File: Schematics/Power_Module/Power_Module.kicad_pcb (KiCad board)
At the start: 4 copper layers, 69.5 x 60 mm, 135 parts, among them J1 ScrewSwitch, J2 Battery, J3 ScrewSwitch, J4 GSE, J5 USB_C_Female_USB2_Small, J6 SWD_B, J7 Stack Male Edge Connector, Q1 AO4447A, Q2 TSM2309CX, Q3 DMN6040SSD-13, SW1 SW_STM_RESET, SW2 SW_STM_BOOT_MODE, U1 TPS61175PWPR, U10 LM66100DCKR, U11 LM66100DCKR, U12 AMS1117-3.3, U13 CP2102N-A02-GQFN20R, U14 STM32F103CBT6, U15 ISO1044BDR, U16 W25Q128JVS, U2 LM74700QDBVRQ1, U3 LM74700QDBVRQ1, U4 ACS37041KLHBLT-010B3, U5 ACS37041KLHBLT-010B5, U6 INA181A2, U7 LMR51430XDDCR, U8 LMR51430XDDCR, U9 LM66100DCKR, Y1 X322516MMB4SI

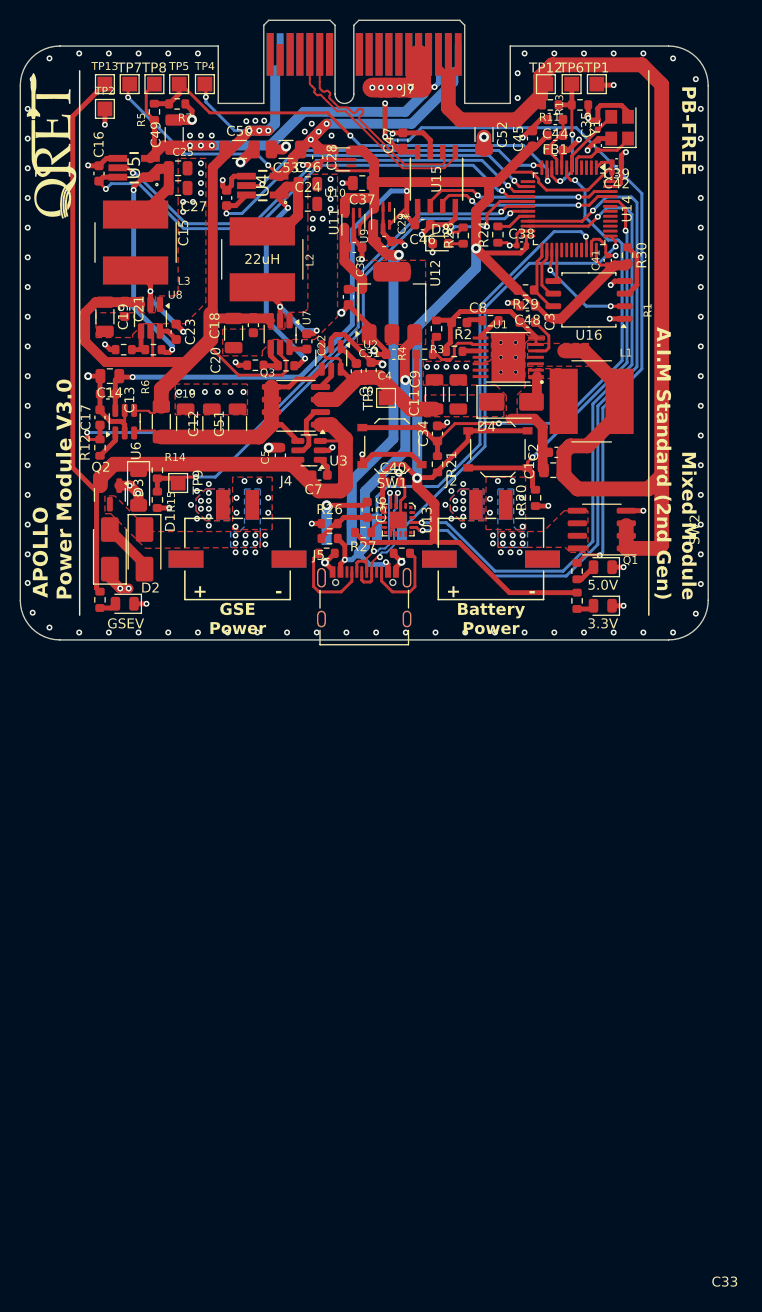
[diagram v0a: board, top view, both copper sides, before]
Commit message: hybrid power board, with preserved OG Power board  - still hybrid still needs review and silkscreen
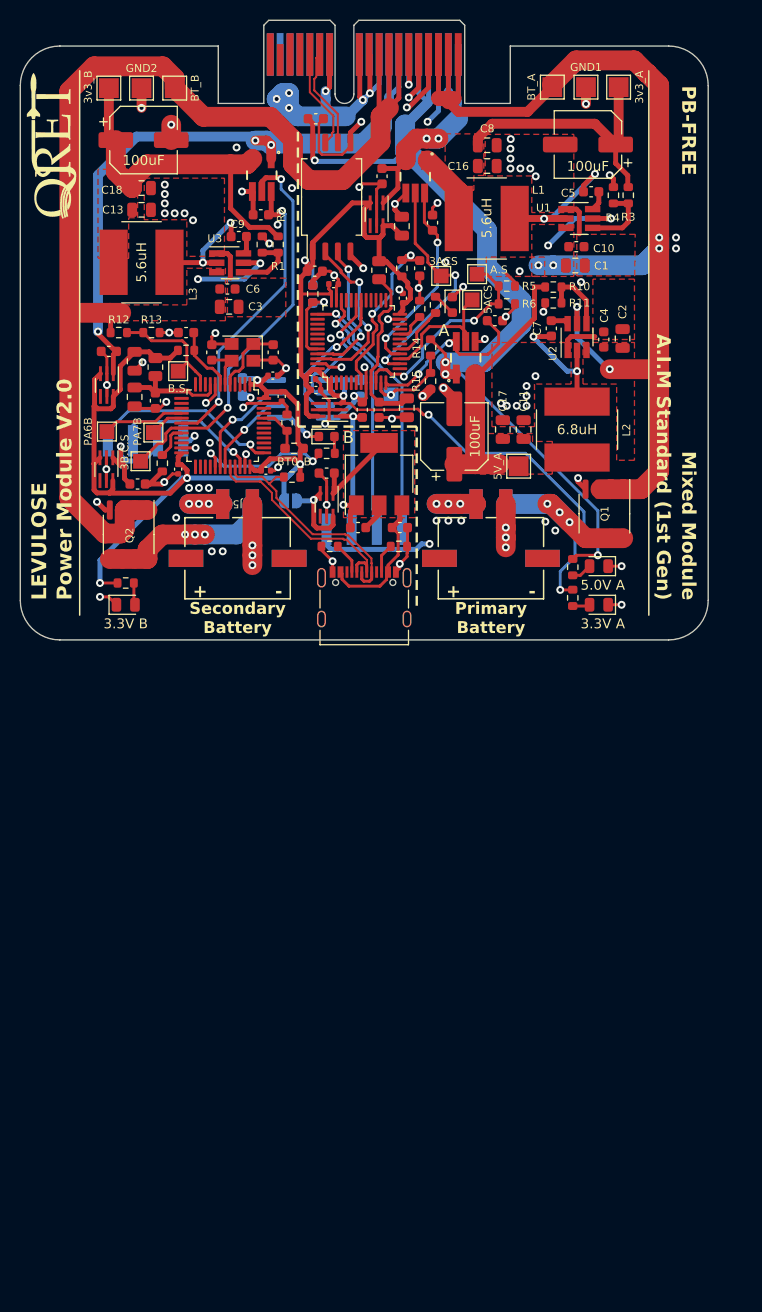
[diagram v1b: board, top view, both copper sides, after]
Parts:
- removed C51, C52, C53: 22uF, Capacitor_SMD:C_1206_3216Metric
- removed D4: 50V 3A, Diode_SMD:D_SMA
- removed D6: 5V PWR (RED), LED_SMD:LED_0805_2012Metric
- removed D7: 24V PWR (YLW), LED_SMD:LED_0805_2012Metric
- removed Q3: DMN6040SSD-13, Package_SO:SOIC-8_3.9x4.9mm_P1.27mm
- removed R29, R30: 10k, Resistor_SMD:R_0603_1608Metric
- removed SW1: SW_STM_RESET, Button_Switch_SMD:SW_Push_1P1T_XKB_TS-1187A
- removed SW2: SW_STM_BOOT_MODE, Button_Switch_SMD:SW_Push_1P1T_XKB_TS-1187A
- added FB2: 100R, Resistor_SMD:R_0805_2012Metric, F.Cu at (143.9, 72.2)
- added J8: SWD_B, SWD_Header:SWD_PinHeader_1x04_P2.54mm_Horizontal_SMD, B.Cu at (161.2, 88.6)
- added JP1: USB_V_EN, Jumper:SolderJumper-2_P1.3mm_Open_RoundedPad1.0x1.5mm, B.Cu at (157.6, 85.7)
- added TP10: B.S, TestPoint:TestPoint_Pad_1.5x1.5mm, F.Cu at (146.2, 72.6)
- added TP11: 3B.C.S, TestPoint:TestPoint_Pad_1.5x1.5mm, F.Cu at (142.4, 81.7)
- added TP16: PA7B, TestPoint:TestPoint_Pad_1.5x1.5mm, F.Cu at (143.7, 78.8)
- added TP17: PA6B, TestPoint:TestPoint_Pad_1.5x1.5mm, F.Cu at (139.0, 78.7)
- C10, C9: value 10uF -> 100nF; footprint Capacitor_SMD:C_1206_3216Metric -> Capacitor_SMD:C_0603_1608Metric
- C11, C18: value 10uF -> 22uF; footprint Capacitor_SMD:C_1206_3216Metric -> Capacitor_SMD:C_0805_2012Metric
- C12: value 22uF -> 100uF; footprint Capacitor_SMD:C_1206_3216Metric -> Capacitor_SMD:CP_Elec_6.3x5.9
- C13, C16, C17: value 100nF -> 22uF; footprint Capacitor_SMD:C_0603_1608Metric -> Capacitor_SMD:C_0805_2012Metric
- C14: value 4.7uF -> 100uF; footprint Capacitor_SMD:C_0805_2012Metric -> Capacitor_SMD:CP_Elec_6.3x5.9
- C15: value 100nF -> 100uF; footprint Capacitor_SMD:C_0603_1608Metric -> Capacitor_SMD:CP_Elec_6.3x5.9
- C19: footprint Capacitor_SMD:C_1206_3216Metric -> Capacitor_SMD:C_0603_1608Metric
- C2: value 100nF -> 4.7uF; footprint Capacitor_SMD:C_0603_1608Metric -> Capacitor_SMD:C_0805_2012Metric
- C20: value 100nF -> 10uF
- C21, C22, C46: value 100nF -> 0.1u
- C23: value 100nF -> 10p
- C24: value 10uF -> 10p; footprint Capacitor_SMD:C_0805_2012Metric -> Capacitor_SMD:C_0603_1608Metric
- C25, C26, C27: value 10uF -> 100n; footprint Capacitor_SMD:C_0805_2012Metric -> Capacitor_SMD:C_0402_1005Metric
- C28, C29, C30: value 1uF -> 100n; footprint Capacitor_SMD:C_0603_1608Metric -> Capacitor_SMD:C_0402_1005Metric
- C3: value 10nF -> 4.7uF; footprint Capacitor_SMD:C_0603_1608Metric -> Capacitor_SMD:C_0805_2012Metric
- C31, C32: value 10uF -> 100n; footprint Capacitor_SMD:C_0603_1608Metric -> Capacitor_SMD:C_0402_1005Metric
- C33: value 10p -> 10n; footprint Capacitor_SMD:C_0402_1005Metric -> Capacitor_SMD:C_0603_1608Metric
- C34: value 100nF -> 1uF; footprint Capacitor_SMD:C_0603_1608Metric -> Capacitor_SMD:C_0805_2012Metric
- C35: value 10p -> 1uF; footprint Capacitor_SMD:C_0402_1005Metric -> Capacitor_SMD:C_0805_2012Metric
- C36: value 1uF -> 10n
- C37, C40: value 10uF -> 1uF
- C38: value 100n -> 1uF; footprint Capacitor_SMD:C_0402_1005Metric -> Capacitor_SMD:C_0805_2012Metric
- C39, C41, C42: value 100n -> 1uF; footprint Capacitor_SMD:C_0402_1005Metric -> Capacitor_SMD:C_0603_1608Metric
- C4, C5, C6, C7: value 1uF -> 100nF
- C43: value 10nF -> 1uF
- C44, C45: value 1uF -> 0.1u
- C49, C50: value 22uF -> 0.1u; footprint Capacitor_SMD:C_1206_3216Metric -> Capacitor_SMD:C_0603_1608Metric_Pad1.08x0.95mm_HandSolder; moved to B.Cu
- C8: value 33nF -> 22uF; footprint Capacitor_SMD:C_0603_1608Metric -> Capacitor_SMD:C_0805_2012Metric
- D1: value SMAJ30A -> 3.3V_A PWR (GRN); footprint Diode_SMD:D_SMA -> LED_SMD:LED_0805_2012Metric
- D2: value SMAJ30A -> 5.0V_A PWR (RED); footprint Diode_SMD:D_SMA -> LED_SMD:LED_0805_2012Metric
- D3: value BZV55C12 -> 3.3V_B PWR (GRN); footprint Diode_SMD:D_MiniMELF -> LED_SMD:LED_0805_2012Metric
- D5: value 3.3V PWR (GRN) -> DB_LED (YLW); footprint LED_SMD:LED_0805_2012Metric -> LED_SMD:LED_0603_1608Metric
- FB1: footprint Inductor_SMD:L_0603_1608Metric -> Resistor_SMD:R_0805_2012Metric
- J1: value ScrewSwitch -> ScrewSwitch B
- J2: value Battery -> ScrewSwitch A; moved to B.Cu
- J3: value ScrewSwitch -> Battery A; moved to F.Cu
- J4: value GSE -> USB_C_Female_USB2_Small; footprint footprints:CONN_2-1445057-2_TYCO -> footprints:USB_C_DB-108PWB
- J5: value USB_C_Female_USB2_Small -> Battery B; footprint footprints:USB_C_DB-108PWB -> footprints:CONN_2-1445057-2_TYCO
- J6: value SWD_B -> Stack Male Edge Connector; footprint SWD_Header:SWD_PinHeader_1x04_P2.54mm_Horizontal_SMD -> Connector_PCBEdge:BUS_PCIexpress_x1; moved to F.Cu
- J7: value Stack Male Edge Connector -> SWD_B; footprint Connector_PCBEdge:BUS_PCIexpress_x1 -> SWD_Header:SWD_PinHeader_1x04_P2.54mm_Horizontal_SMD; moved to B.Cu
- L1: value 47uH -> 5.6uH
- L2: value 22uH -> 6.8uH
- L3: value 68uH -> 5.6uH
- Q2: value TSM2309CX -> AO4447A; footprint Package_TO_SOT_SMD:SOT-23 -> Package_SO:SOIC-8_3.9x4.9mm_P1.27mm
- R1: value 6.2k -> 100k
- R10: value 12K -> 56k
- R11: value 30k -> 7.5k
- R12: value 1k -> 30k
- R14: value 10k -> 30k
- R15: value 100k -> 30k
- R16: value 100k -> 1.5k
- R17: value 22k -> 5.1k
- R18: value 56k -> 5.1k
- R19: value 7.5k -> 680R
- R2: value 82k -> 22k
- R20: value 100k -> 680R
- R21: value 100k -> 10k
- R22: value 5.1k -> 10k
- R23: value 5.1k -> 100k
- R24: value 100k -> BT0_A; footprint Resistor_SMD:R_0603_1608Metric -> Resistor_SMD:R_0603_1608Metric_Pad0.98x0.95mm_HandSolder; moved to B.Cu
- R25: value 22k -> 100k
- R26: value 47k -> 100k
- R27: value 1k -> BT0_B; footprint Resistor_SMD:R_0603_1608Metric -> Resistor_SMD:R_0603_1608Metric_Pad0.98x0.95mm_HandSolder
- R28: value 680R -> 100k
- R3: value 12k -> 100k
- R4: value 220k -> 22k
- R6: value 100m -> 10k; footprint Resistor_SMD:R_1206_3216Metric_Pad1.30x1.75mm_HandSolder -> Resistor_SMD:R_0603_1608Metric
- R7: value 30k -> 3.3k
- R8: value 3.3k -> 2.4k
- R9: value 2.4k -> 3.3k
- TP1: value BATT_GND1 -> BT_A; footprint TestPoint:TestPoint_Pad_1.5x1.5mm -> TestPoint:TestPoint_Pad_2.0x2.0mm
- TP12: value BATT -> 3ACS
- TP13: value GSEV -> 5ACS
- TP2: value GSE_GND1 -> BT_B; footprint TestPoint:TestPoint_Pad_1.5x1.5mm -> TestPoint:TestPoint_Pad_2.0x2.0mm
- TP3: value 24V_PSU -> GND2; footprint TestPoint:TestPoint_Pad_1.5x1.5mm -> TestPoint:TestPoint_Pad_2.0x2.0mm
- TP4: value 24V_MUX -> GND1; footprint TestPoint:TestPoint_Pad_1.5x1.5mm -> TestPoint:TestPoint_Pad_2.0x2.0mm
- TP5: value 5VSENS -> 3v3_A; footprint TestPoint:TestPoint_Pad_1.5x1.5mm -> TestPoint:TestPoint_Pad_2.0x2.0mm
- TP6: value A.S -> 5V_A; footprint TestPoint:TestPoint_Pad_1.5x1.5mm -> TestPoint:TestPoint_Pad_2.0x2.0mm
- TP7: value 3v3 -> 3v3_B; footprint TestPoint:TestPoint_Pad_1.5x1.5mm -> TestPoint:TestPoint_Pad_2.0x2.0mm
- TP8: value 5V -> 5VSENS; moved to B.Cu
- TP9: value GSE_SENS -> A.S
- U1: value TPS61175PWPR -> LMR51430XDDCR; footprint footprints:IC_TPS27S100BPWPR -> Package_TO_SOT_SMD:SOT-23-6_Handsoldering
- U10: value LM66100DCKR -> ISO1042BDWVR; footprint LMR66100:SC-70-6 -> ISO1042:SOIC-8 ISO1042BDWV
- U11: footprint LMR66100:SC-70-6 -> LMR66100:SC-70-6_Handsoldering
- U12: value AMS1117-3.3 -> LM66100DCKR; footprint Package_TO_SOT_SMD:SOT-223-3_TabPin2 -> LMR66100:SC-70-6_Handsoldering
- U13: value CP2102N-A02-GQFN20R -> LM66100DCKR; footprint digikey-footprints:QFN-20-1EP_3x3mm -> LMR66100:SC-70-6_Handsoldering
- U14: value STM32F103CBT6 -> LM66100DCKR; footprint Package_QFP:LQFP-48_7x7mm_P0.5mm -> LMR66100:SC-70-6_Handsoldering
- U15: value ISO1044BDR -> LM66100DCKR; footprint ISO1044:SOIC_1044BDR_TEX -> LMR66100:SC-70-6_Handsoldering
- U16: value W25Q128JVS -> SCM3721ASA; footprint Package_SO:SOIC-8_5.23x5.23mm_P1.27mm -> Package_SO:SOIC-8_3.9x4.9mm_P1.27mm; moved to B.Cu
- U2, U3: value LM74700QDBVRQ1 -> LMR51430XDDCR; footprint Package_TO_SOT_SMD:SOT-23-6 -> Package_TO_SOT_SMD:SOT-23-6_Handsoldering
- U4: value ACS37041KLHBLT-010B3 -> STM32F103C8T6; footprint footprints:APS12628LLHALTBAP_HandSolder -> Package_QFP:LQFP-48_7x7mm_P0.5mm
- U5: value ACS37041KLHBLT-010B5 -> STM32F103C8T6; footprint footprints:APS12628LLHALTBAP_HandSolder -> Package_QFP:LQFP-48_7x7mm_P0.5mm
- U6: value INA181A2 -> ACS37041KLHBLT-010B3; footprint Package_TO_SOT_SMD:SOT-23-6 -> footprints:APS12628LLHALTBAP_HandSolder
- U7, U8: value LMR51430XDDCR -> ACS37041KLHBLT-010B3; footprint Package_TO_SOT_SMD:SOT-23-6_Handsoldering -> footprints:APS12628LLHALTBAP_HandSolder
- U9: value LM66100DCKR -> AMS1117-3.3; footprint LMR66100:SC-70-6 -> Package_TO_SOT_SMD:SOT-223-3_TabPin2
- moved R7 63.9 mm to (186.1, 95.5), turned to -90 degrees
- moved R10 55.6 mm to (184.1, 64.1), turned to 0 degrees
- moved C39 54.7 mm to (139.2, 70.6)
- moved C41 52.6 mm to (142.1, 84.0), turned to 0 degrees
- moved J6 49.8 mm to (174.5, 40.6), turned to 180 degrees
- moved D2 49.4 mm to (188.7, 92.3), turned to 180 degrees
- moved R13 49.0 mm to (143.5, 68.7)
- moved J7 47.9 mm to (146.7, 79.6), turned to 90 degrees
- moved C12 47.3 mm to (187.6, 49.7), turned to 180 degrees
- moved D1 46.2 mm to (188.7, 96.2), turned to 180 degrees
- moved R9 45.6 mm to (140.9, 94.0), turned to 0 degrees
- moved TP5 44.4 mm to (190.7, 43.9)
- moved Y1 44.3 mm to (152.7, 70.7), turned to 180 degrees
- moved C10 43.3 mm to (186.4, 60.0), turned to 0 degrees
- moved TP13 43.0 mm to (175.9, 65.4)
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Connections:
- C1 pad 1: V_BATT -> BATT_A
- C10 pad 1: 24V_MUX_Pre -> BATT_A
- C11 pad 1: 24V_PSU -> 5.0V_A_Pre
- C12 pad 1: 24V_MUX_Pre -> 3.3V_A_Pre
- C13 pad 1: 3.3V_MUX -> 3.3V_B_Pre
- C13 pad 2: GND -> GND2
- C14 pad 1: 3.3V_MUX -> 5.0V_A_Pre
- C15 pad 1: 3.3V_ACS_PWR -> 3.3V_B_Pre
- C15 pad 2: GND -> GND2
- C16 pad 1: 5V_ACS_PWR -> 3.3V_A_Pre
- C17 pad 1: 24V_CURR_SENSE -> 5.0V_A_Pre
- C18 pad 1: 24V_MUX -> 3.3V_B_Pre
- C18 pad 2: GND -> GND2
- C19 pad 1: 24V_MUX -> Net-(U9-VI)
- C19 pad 2: GND -> GND2
- C2 pad 1: V_BATT -> BATT_A
- C20 pad 1: 24V_MUX -> V_REGUSB_B
- C20 pad 2: GND -> GND2
- C21 pad 1: 24V_MUX -> GND
- C21 pad 2: GND -> V_MUX_A
- C22 pad 1: Net-(U7-CB) -> GND
- C22 pad 2: Net-(U7-SW) -> 5.0V_A
- C23 pad 1: Net-(U8-SW) -> OSC_IN
- C23 pad 2: Net-(U8-CB) -> GND2
- C24 pad 1: 3.3V_PSU_Pre -> OSC_OUT
- C24 pad 2: GND -> GND2
- C25 pad 1: 5V_PSU_Pre -> GND2
- C25 pad 2: GND -> V_MUX_B
- C26 pad 1: 3.3V_PSU_Pre -> GND
- C26 pad 2: GND -> V_MUX_A
- C27 pad 1: 5V_PSU_Pre -> GND
- C27 pad 2: GND -> V_MUX_A
- C28 pad 1: 3.3V_PSU -> GND
- C28 pad 2: GND -> V_MUX_A
- C29 pad 1: 3.3V_SWD -> GND
- C29 pad 2: GND -> V_MUX_A
- C3 pad 1: Net-(U1-SS) -> BATT_B
- C3 pad 2: GND -> GND2
- C30 pad 1: 3.3V_REGUSB -> GND2
- C30 pad 2: GND -> V_MUX_B
- C31 pad 1: 5V_USB -> GND2
- C31 pad 2: GND -> V_MUX_B
- C32 pad 1: 3.3V_REGUSB -> GND2
- C32 pad 2: GND -> V_MUX_B
- C33 pad 1: OSC_IN -> 3.3VA_A
- C34 pad 1: STM_RESET -> 3.3VA_A
- C35 pad 1: OSC_OUT -> V_MUX_A
- C36 pad 1: GND -> 3.3VA_B
- C36 pad 2: Net-(U13-VBUS) -> GND2
- C37 pad 1: 3.3V_MUX -> 3.3VA_B
- C37 pad 2: GND -> GND2
- C38 pad 1: GND -> V_MUX_B
- C38 pad 2: 3.3V_MUX -> GND2
- C39 pad 1: GND -> 3.3V_B
- C39 pad 2: 3.3V_MUX -> GND2
- C4 pad 1: GND -> BATT_A
- C4 pad 2: 24V_PSU -> GND
- C40 pad 1: 3.3V_MUX -> V_REGUSB_B
- C40 pad 2: GND -> GND2
- C41 pad 1: GND -> V_SWD_B
- C41 pad 2: 3.3V_MUX -> GND2
- C42 pad 1: GND -> 3.3V_A
- C42 pad 2: 3.3V_MUX -> GND
- C43 pad 1: 3.3VA -> V_SWD_A
- C44 pad 1: 3.3VA -> 3.3V_A_ACS_PWR
- C45 pad 1: 3.3V_MUX -> 5.0V_A_ACS_PWR
- C46 pad 1: 3.3V_MUX -> 3.3V_B_ACS_PWR
- C46 pad 2: GND -> GND2
- C47 pad 1: 5V_PSU -> STM_RESET_B
- C47 pad 2: GND -> GND2
- C48 pad 1: 3.3V_MUX -> STM_RESET_A
- C49 pad 1: 5V_PSU -> GND
- C49 pad 2: GND -> V_MUX_A
- C5 pad 1: 24V_GSE -> Net-(U1-SW)
- C5 pad 2: GND -> Net-(U1-CB)
- C50 pad 1: 24V_MUX -> V_MUX_B
- C50 pad 2: GND -> GND2
- C6 pad 1: Net-(U2-VCAP) -> BATT_B
- C6 pad 2: 24V_PSU -> GND2
- C7 pad 1: 24V_GSE -> Net-(U2-SW)
- C7 pad 2: Net-(U3-VCAP) -> Net-(U2-CB)
- C8 pad 1: Net-(C8-Pad1) -> 3.3V_A_Pre
- C9 pad 1: 24V_PSU -> Net-(U3-SW)
- C9 pad 2: GND -> Net-(U3-CB)
- D1 pad 1: /power/GSE_SW+ -> GND
- D1 pad 2: Net-(D1-A2) -> Net-(D1-A)
- D2 pad 2: Net-(D1-A2) -> Net-(D2-A)
- D3 pad 1: 24V_GSE -> GND2
- D3 pad 2: GND -> Net-(D3-A)
- D8 pad 1: GND -> GND2
- FB1 pad 1: 3.3VA -> 3.3VA_A
- FB1 pad 2: 3.3V_MUX -> V_MUX_A
- J1 pad 1: /power/BATT+ -> Net-(J1-Pad1)
- J1 pad 2: /power/BATT_SW+ -> Net-(J1-Pad2)
- J2 pad 1: GND -> Net-(J2-Pad1)
- J2 pad 2: /power/BATT+ -> Net-(J2-Pad2)
- J3 pad 1: /power/GSE+ -> GND
- J3 pad 2: /power/GSE_SW+ -> Net-(J2-Pad1)
- L1 pad 1: V_BATT -> Net-(U1-SW)
- L1 pad 2: /power/BOOST_SW -> 3.3V_A_Pre
- L2 pad 1: 3.3V_PSU_Pre -> Net-(U2-SW)
- L2 pad 2: Net-(U7-SW) -> 5.0V_A_Pre
- L3 pad 1: Net-(U8-SW) -> Net-(U3-SW)
- L3 pad 2: 5V_PSU_Pre -> 3.3V_B_Pre
- Q1 pad 1: V_BATT -> BATT_A
- Q1 pad 2: V_BATT -> BATT_A
- Q1 pad 3: V_BATT -> BATT_A
- Q1 pad 5: /power/BATT_SW+ -> Net-(J2-Pad2)
- Q1 pad 6: /power/BATT_SW+ -> Net-(J2-Pad2)
- Q1 pad 7: /power/BATT_SW+ -> Net-(J2-Pad2)
- Q1 pad 8: /power/BATT_SW+ -> Net-(J2-Pad2)
- Q2 pad 1: GND -> BATT_B
- Q2 pad 2: 24V_GSE -> BATT_B
- Q2 pad 3: /power/GSE_SW+ -> BATT_B
- R1 pad 1: Net-(U1-COMP) -> 3.3V_B_Pre
- R1 pad 2: Net-(C8-Pad1) -> Net-(U3-FB)
- R10 pad 1: 24V_GSE -> 5.0V_A_Pre
- R10 pad 2: Net-(D7-A) -> Net-(U2-FB)
- R11 pad 1: V_BATT -> Net-(U2-FB)
- R11 pad 2: BATT_SENSE -> GND
- R12 pad 1: 24V_CURR_SENSE -> BATT_B
- R12 pad 2: Net-(R12-Pad2) -> BATT_B_SENSE
- R13 pad 1: BATT_SENSE -> BATT_B_SENSE
- R13 pad 2: GND -> GND2
- R14 pad 1: GSE_SENSE -> 5.0V_A
- R14 pad 2: 24V_GSE -> 5.0V_A_SENSE
- R15 pad 1: GSE_SENSE -> 5.0V_A_SENSE
- R16 pad 1: 3.3V_PSU_Pre -> V_MUX_B
- R16 pad 2: Net-(U7-FB) -> USB_D+
- R17 pad 1: Net-(U7-FB) -> Net-(J4-CC1)
- R17 pad 2: GND -> GND2
- R18 pad 1: 5V_PSU_Pre -> Net-(J4-CC2)
- R18 pad 2: Net-(U8-FB) -> GND2
- R19 pad 1: Net-(U8-FB) -> Net-(D5-A)
- R19 pad 2: GND -> DB_LED_A
- R2 pad 1: Net-(U1-FREQ) -> Net-(U3-FB)
- R2 pad 2: GND -> GND2
- R20 pad 1: GND -> Net-(D8-A)
- R20 pad 2: BOOT0 -> DB_LED_B
- R21 pad 1: STM_RESET -> STM_RESET_B
- R21 pad 2: 3.3V_MUX -> V_MUX_B
- R22 pad 1: Net-(J5-CC1) -> STM_RESET_A
- R22 pad 2: GND -> V_MUX_A
- R23 pad 1: Net-(J5-CC2) -> GND
- R23 pad 2: GND -> BOOT0_A
- R24 pad 1: GND -> V_MUX_A
- R24 pad 2: BOOT1 -> BOOT0_A
- R25 pad 1: Net-(U13-VBUS) -> GND
- R25 pad 2: 5V_USB -> BOOT1_A
- R26 pad 1: GND -> GND2
- R26 pad 2: Net-(U13-VBUS) -> BOOT0_B
- R27 pad 1: Net-(U13-~{RST}) -> V_MUX_B
- R27 pad 2: 3.3V_MUX -> BOOT0_B
- R28 pad 1: Net-(D8-A) -> GND2
- R28 pad 2: DB_LED -> BOOT1_B
- R3 pad 1: Net-(U1-FB) -> 3.3V_A_Pre
- R3 pad 2: GND -> Net-(U1-FB)
- R4 pad 1: 24V_PSU -> Net-(U1-FB)
- R4 pad 2: Net-(U1-FB) -> GND
- R5 pad 1: 5V_PSU -> BATT_A
- R5 pad 2: 5V_SENSE -> BATT_A_SENSE
- R6 pad 1: 24V_MUX_Pre -> BATT_A_SENSE
- R6 pad 2: 24V_MUX -> GND
- R7 pad 1: 5V_SENSE -> V_MUX_A
- R7 pad 2: GND -> Net-(D1-A)
- R8 pad 1: 3.3V_MUX -> 5.0V_A
- R8 pad 2: Net-(D5-A) -> Net-(D2-A)
- R9 pad 1: 5V_PSU -> V_MUX_B
- R9 pad 2: Net-(D6-A) -> Net-(D3-A)
- TP1 pad 1: GND -> BATT_A
- TP12 pad 1: V_BATT -> 3.3V_A_CURR_SENSE
- TP13 pad 1: 24V_GSE -> 5.0V_A_CURR_SENSE
- TP2 pad 1: GND -> BATT_B
- TP3 pad 1: 24V_PSU -> GND2
- TP4 pad 1: 24V_MUX -> GND
- TP5 pad 1: 5V_SENSE -> 3.3V_A_Pre
- TP6 pad 1: BATT_SENSE -> 5.0V_A_Pre
- TP7 pad 1: 3.3V_PSU -> 3.3V_B_Pre
- TP8 pad 1: 5V_PSU -> 5.0V_A_SENSE
- TP9 pad 1: GSE_SENSE -> BATT_A_SENSE
- U1 pad 1: /power/BOOST_SW -> GND
- U1 pad 2: /power/BOOST_SW -> Net-(U1-SW)
- U1 pad 3: V_BATT -> BATT_A
- U1 pad 4: V_BATT -> Net-(U1-FB)
- U1 pad 5: Net-(U1-SS) -> BATT_A
- U1 pad 6: GND -> Net-(U1-CB)
- U10 pad 1: 3.3V_SWD -> V_MUX_A
- U10 pad 2: GND -> CAN_TX
- U10 pad 3: 3.3V_MUX -> CAN_RX
- U10 pad 4: unconnected-(U10-NC-Pad4) -> GND
- U10 pad 6: 3.3V_MUX -> CAN_-
- U11 pad 1: 3.3V_REGUSB -> 3.3V_B
- U11 pad 2: GND -> GND2
- U11 pad 3: 3.3V_MUX -> V_MUX_B
- U11 pad 5: GND -> GND2
- U11 pad 6: 3.3V_MUX -> V_MUX_B
- U12 pad 1: GND -> V_REGUSB_B
- U12 pad 2: 3.3V_REGUSB -> GND2
- U12 pad 3: 5V_USB -> Net-(JP1-B)
- U13 pad 1: unconnected-(U13-RS485/GPIO.1-Pad1) -> V_SWD_B
- U13 pad 2: unconnected-(U13-CLK/GPIO.0-Pad2)_1 -> GND2
- U13 pad 3: GND -> V_MUX_B
- U13 pad 4: USB_P -> unconnected-(U13-NC-Pad4)
- U13 pad 5: USB_N -> GND2
- U13 pad 6: 3.3V_MUX -> V_MUX_B
- U14 pad 1: 3.3V_MUX -> 3.3V_A
- U14 pad 2: unconnected-(U14-PC13-Pad2) -> GND
- U14 pad 3: unconnected-(U14-PC14-Pad3) -> V_MUX_A
- U14 pad 5: OSC_IN -> GND
- U14 pad 6: OSC_OUT -> V_MUX_A
- U15 pad 1: 3.3V_MUX -> V_SWD_A
- U15 pad 2: CAN_TX -> GND
- U15 pad 3: CAN_RX -> V_MUX_A
- U15 pad 4: GND -> unconnected-(U15-NC-Pad4)
- U15 pad 5: CAN_N -> GND
- U15 pad 6: CAN_P -> V_MUX_A
- U16 pad 1: GND -> V_MUX_A
- U16 pad 2: MISO_FL -> RX_A
- U16 pad 3: Net-(U16-IO2) -> TX_A
- U16 pad 5: MOSI_FL -> GND2
- U16 pad 6: SCK_FL -> RX_B
- U16 pad 7: RESET_FL -> TX_B
- U16 pad 8: 3.3V_MUX -> V_MUX_B
- U2 pad 1: Net-(U2-VCAP) -> GND
- U2 pad 2: GND -> Net-(U2-SW)
- U2 pad 3: 24V_PSU -> BATT_A
- U2 pad 4: 24V_MUX_Pre -> Net-(U2-FB)
- U2 pad 5: Net-(Q3B-G2) -> BATT_A
- U2 pad 6: 24V_PSU -> Net-(U2-CB)
- U3 pad 1: Net-(U3-VCAP) -> GND2
- U3 pad 2: GND -> Net-(U3-SW)
- U3 pad 3: 24V_GSE -> BATT_B
- U3 pad 4: 24V_MUX_Pre -> Net-(U3-FB)
- U3 pad 5: Net-(Q3A-G1) -> BATT_B
- U3 pad 6: 24V_GSE -> Net-(U3-CB)
- U4 pad 1: 3.3V_PSU_Pre -> V_MUX_A
- U4 pad 2: 3.3V_PSU -> unconnected-(U4-PC13-Pad2)
- U4 pad 3: GND -> unconnected-(U4-PC14-Pad3)
- U4 pad 4: 3.3V_CURR_SENSE -> unconnected-(U4-PC15-Pad4)
- U4 pad 5: 3.3V_ACS_PWR -> unconnected-(U4-PD0-Pad5)
- U5 pad 1: 5V_PSU_Pre -> V_MUX_B
- U5 pad 2: 5V_PSU -> unconnected-(U5-PC13-Pad2)
- U5 pad 3: GND -> unconnected-(U5-PC14-Pad3)
- U5 pad 4: 5V_CURR_SENSE -> unconnected-(U5-PC15-Pad4)
- U5 pad 5: 5V_ACS_PWR -> OSC_IN
- U6 pad 1: Net-(R12-Pad2) -> 3.3V_A_Pre
- U6 pad 2: GND -> 3.3V_A
- U6 pad 3: 24V_MUX_Pre -> GND
- U6 pad 4: 24V_MUX -> 3.3V_A_CURR_SENSE
- U6 pad 5: GND -> 3.3V_A_ACS_PWR
- U7 pad 1: GND -> 5.0V_A
- U7 pad 2: Net-(U7-SW) -> 5.0V_A_Pre
- U7 pad 3: 24V_MUX -> GND
- U7 pad 4: Net-(U7-FB) -> 5.0V_A_CURR_SENSE
- U7 pad 5: 24V_MUX -> 5.0V_A_ACS_PWR
- U8 pad 1: GND -> 3.3V_B
- U8 pad 2: Net-(U8-SW) -> 3.3V_B_Pre
- U8 pad 3: 24V_MUX -> GND2
- U8 pad 4: Net-(U8-FB) -> 3.3V_B_CURR_SENSE
- U8 pad 5: 24V_MUX -> 3.3V_B_ACS_PWR
- U9 pad 1: 3.3V_PSU -> GND2
- U9 pad 2: GND -> V_REGUSB_B
- U9 pad 3: 3.3V_MUX -> Net-(U9-VI)
- Y1 pad 2: GND -> GND2
- Y1 pad 4: GND -> GND2
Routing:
- net 3.3V_MUX: track 228.1 -> 0.00 mm, vias 4 -> 0
- net BATT_B: track 0.00 -> 130.2 mm, vias 0 -> 2
- net BATT_A: track 0.00 -> 125.8 mm, vias 0 -> 8
- net 5V_PSU: track 125.3 -> 0.00 mm, vias 6 -> 0
- net GND2: track 0.00 -> 121.7 mm, vias 0 -> 52
- net V_BATT: track 114.7 -> 0.00 mm
- net V_MUX_A: track 0.00 -> 106.3 mm, vias 0 -> 4
- net V_MUX_B: track 0.00 -> 97.9 mm, vias 0 -> 4
- net 5.0V_A: track 0.00 -> 97.4 mm, vias 0 -> 4
- net 24V_MUX: track 94.7 -> 0.00 mm, vias 4 -> 0
- net GND: track 214.5 -> 122.0 mm, vias 198 -> 58
- net 24V_GSE: track 92.5 -> 0.00 mm
- net USART_TX: track 70.5 -> 0.00 mm, vias 2 -> 0
- net 3.3V_B: track 0.00 -> 68.0 mm, vias 0 -> 3
- net USART_RX: track 67.7 -> 0.00 mm, vias 2 -> 0
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- added copper zone on F.Cu, net 3.3V_A_Pre
- added copper zone on F.Cu, net 3.3V_B_Pre
- added copper zone on F.Cu, net 5.0V_A_Pre
- added copper zone on F.Cu, net BATT_A
- added copper zone on F.Cu, net BATT_B
- added copper zone on F.Cu, net GND2
- added copper zone on In1.Cu, net GND2
- added copper zone on In2.Cu, net GND2
- added copper zone on F.Cu, net V_REGUSB_B
- removed copper zone on B.Cu, net /power/BATT+
- removed copper zone on F.Cu, net /power/BATT+
- removed copper zone on B.Cu, net /power/BATT_SW+
- removed copper zone on F.Cu, net /power/BATT_SW+
- removed copper zone on F.Cu, net /power/BOOST_SW
- removed copper zone on B.Cu, net /power/GSE+
- removed copper zone on F.Cu, net /power/GSE+
- removed copper zone on B.Cu, net /power/GSE_SW+
- removed copper zone on F.Cu, net /power/GSE_SW+
- removed copper zone on F.Cu, net 24V_PSU
- removed copper zone on F.Cu, net 3.3V_REGUSB
- removed copper zone on F.Cu, net V_BATT
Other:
- board text added: "3.3V A"
- board text added: "3.3V B"
- board text added: "5.0V A"
- board text added: "A"
- board text added: "A.I.M Standard (1st Gen)"
- board text added: "B"
- board text added: "LEVULOSE"
- board text added: "Power Module Rev 2.0 QRET Mar 2025 Rajan Laird Kennan Bays Oak Campbell"
- board text added: "Power Module V2.0"
- board text added: "Primary Battery"
- board text added: "Primary Switch"
- board text added: "Secondary Battery"
- board text added: "Secondary Switch"
- board text removed: "3.3V"
- board text removed: "5.0V"
- board text removed: "A.I.M Standard (2nd Gen)"
- board text removed: "APOLLO"
- board text removed: "Battery Power"
- board text removed: "Battery Switch"
- board text removed: "GSE Power"
- board text removed: "GSE Switch"
- board text removed: "GSEV"
- board text removed: "Power Module Rev 3.0 QRET Mar 2026 Rajan Laird, Kennan Bays Oak Campbell, Tristan Alderson"
- board text removed: "Power Module V3.0"

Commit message: init commit of power board hybrid revision
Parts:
- removed C13, C18: 22uF, Capacitor_SMD:C_0805_2012Metric
- removed C15: 100uF, Capacitor_SMD:CP_Elec_6.3x5.9
- removed C23, C24: 10p, Capacitor_SMD:C_0603_1608Metric
- removed C25, C30, C31, C32: 100n, Capacitor_SMD:C_0402_1005Metric
- removed C3: 4.7uF, Capacitor_SMD:C_0805_2012Metric
- removed C36: 10n, Capacitor_SMD:C_0603_1608Metric
- removed C37, C38: 1uF, Capacitor_SMD:C_0805_2012Metric
- removed C39, C41: 1uF, Capacitor_SMD:C_0603_1608Metric
- removed C46: 0.1u, Capacitor_SMD:C_0603_1608Metric
- removed C47, C6, C9: 100nF, Capacitor_SMD:C_0603_1608Metric
- removed C49, C50: 0.1u, Capacitor_SMD:C_0603_1608Metric_Pad1.08x0.95mm_HandSolder
- removed D3: 3.3V_B PWR (GRN), LED_SMD:LED_0805_2012Metric
- removed D8: DB_LED (YLW), LED_SMD:LED_0603_1608Metric
- removed FB2: 100R, Resistor_SMD:R_0805_2012Metric
- removed J1: ScrewSwitch B, footprints:CONN_2-1445057-2_TYCO
- removed J5: Battery B, footprints:CONN_2-1445057-2_TYCO
- removed J7: SWD_B, SWD_Header:SWD_PinHeader_1x04_P2.54mm_Horizontal_SMD
- removed JP1: USB_V_EN, Jumper:SolderJumper-2_P1.3mm_Open_RoundedPad1.0x1.5mm
- removed L3: 5.6uH, Inductor_SMD:L_Bourns_SRN8040TA
- removed Q2: AO4447A, Package_SO:SOIC-8_3.9x4.9mm_P1.27mm
- removed R1, R26, R28: 100k, Resistor_SMD:R_0603_1608Metric
- removed R12: 30k, Resistor_SMD:R_0603_1608Metric
- removed R13, R21: 10k, Resistor_SMD:R_0603_1608Metric
- removed R2: 22k, Resistor_SMD:R_0603_1608Metric
- removed R20: 680R, Resistor_SMD:R_0603_1608Metric
- removed R27: BT0_B, Resistor_SMD:R_0603_1608Metric_Pad0.98x0.95mm_HandSolder
- removed R9: 3.3k, Resistor_SMD:R_0603_1608Metric
- removed TP10: B.S, TestPoint:TestPoint_Pad_1.5x1.5mm
- removed TP11: 3B.C.S, TestPoint:TestPoint_Pad_1.5x1.5mm
- removed TP16: PA7B, TestPoint:TestPoint_Pad_1.5x1.5mm
- removed TP17: PA6B, TestPoint:TestPoint_Pad_1.5x1.5mm
- removed TP2: BT_B, TestPoint:TestPoint_Pad_2.0x2.0mm
- removed TP3: GND2, TestPoint:TestPoint_Pad_2.0x2.0mm
- removed TP7: 3v3_B, TestPoint:TestPoint_Pad_2.0x2.0mm
- removed U11, U13: LM66100DCKR, LMR66100:SC-70-6_Handsoldering
- removed U16: SCM3721ASA, Package_SO:SOIC-8_3.9x4.9mm_P1.27mm
- removed U3: LMR51430XDDCR, Package_TO_SOT_SMD:SOT-23-6_Handsoldering
- removed U5: STM32F103C8T6, Package_QFP:LQFP-48_7x7mm_P0.5mm
- removed U8: ACS37041KLHBLT-010B3, footprints:APS12628LLHALTBAP_HandSolder
- removed Y1: X322516MMB4SI, Crystal:Crystal_SMD_3225-4Pin_3.2x2.5mm
- R16: value 1.5k -> 5.1k
- R18: value 5.1k -> 1.5k
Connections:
- net 3.3V_B renamed Net-(J6-3.3V_B-PadA7)
- net BATT_B renamed Net-(J6-BATT_B-PadB7)
- net V_SWD_A renamed 3.3V_SWD_A
- C19 pad 2: GND2 -> GND
- C20 pad 1: V_REGUSB_B -> V_REGUSB_A
- C20 pad 2: GND2 -> GND
- C21 pad 2: V_MUX_A -> 3.3V_MUX_A
- C40 pad 1: V_REGUSB_B -> 3.3V_REGUSB_A
- J6 pad A12: GND2 -> Net-(J6-GND_B-PadA12)
- J6 pad A9: GND2 -> Net-(J6-GND_B-PadA12)
- J6 pad B10: GND2 -> Net-(J6-GND_B-PadA12)
- J6 pad B11: GND2 -> Net-(J6-GND_B-PadA12)
- J6 pad B12: GND2 -> Net-(J6-GND_B-PadA12)
- R16 pad 1: V_MUX_B -> Net-(J4-CC1)
- R16 pad 2: USB_D+ -> GND2
- R17 pad 1: Net-(J4-CC1) -> Net-(J4-CC2)
- R18 pad 1: Net-(J4-CC2) -> 3.3V_MUX_A
- R18 pad 2: GND2 -> USB_D+
- U10 pad 1: V_MUX_A -> 3.3V_MUX_A
- U12 pad 1: V_REGUSB_B -> 3.3V_REGUSB_A
- U12 pad 3: Net-(JP1-B) -> 3.3V_MUX_A
- U12 pad 6: Net-(JP1-B) -> 3.3V_MUX_A
- U14 pad 3: V_MUX_A -> 3.3V_MUX_A
- U14 pad 6: V_MUX_A -> 3.3V_MUX_A
- U15 pad 3: V_MUX_A -> 3.3V_MUX_A
- U15 pad 6: V_MUX_A -> 3.3V_MUX_A
- U9 pad 1: GND2 -> GND
- U9 pad 2: V_REGUSB_B -> V_REGUSB_A
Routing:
- net (no net): track 0.00 -> 274.4 mm, vias 0 -> 19
- net Net-(J4-CC1): track 3.18 -> 101.1 mm, vias 0 -> 4
- net V_MUX_B: track 97.9 -> 0.00 mm, vias 4 -> 0
- net 3.3V_B_CURR_SENSE: track 40.9 -> 0.00 mm, vias 2 -> 0
- net GND2: track 121.7 -> 81.2 mm, vias 52 -> 45
- net Net-(J6-GND_B-PadA12): track 0.00 -> 36.7 mm, vias 0 -> 6
- net Net-(J6-3.3V_B-PadA7): track 68.0 -> 103.4 mm
- net 3.3V_B_Pre: track 35.4 -> 0.00 mm
- net 3.3V_B_ACS_PWR: track 30.9 -> 0.00 mm, vias 2 -> 0
- net Net-(J1-Pad2): track 20.2 -> 0.00 mm, vias 3 -> 0
- net SWCLK_B: track 19.5 -> 0.00 mm, vias 1 -> 0
- net SWDIO_B: track 14.9 -> 0.00 mm, vias 1 -> 0
- net DB_LED_B: track 14.3 -> 0.00 mm, vias 2 -> 0
- net BATT_B_SENSE: track 12.3 -> 0.00 mm
- net V_REGUSB_B: track 11.9 -> 0.00 mm
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- added copper zone on F.Cu, net Net-(J6-3.3V_B-PadA7)
- added copper zone on F.Cu, net V_REGUSB_A
- removed copper zone on F.Cu, net 3.3V_B_Pre
- removed copper zone on F.Cu, net V_REGUSB_B
